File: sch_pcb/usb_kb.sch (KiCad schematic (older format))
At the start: 44 parts, among them J1 Conn_01x04_Female, P1 USB_C_Plug, SW1 SW_Push, SW2 SW_Push, U1 STM32F103C6Tx, U2 USBLC6-2SC6, U3 AMS1117-3.3, X1 8MHz

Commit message: Новые посадочные места
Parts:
- C1, C10, C11, C12, C13, C14, C15, C2, C3, C4, C5, C6, C7, C8, C9: footprint Capacitor_SMD:C_0805_2012Metric_Pad1.15x1.40mm_HandSolder -> Capacitor_SMD:C_0805_2012Metric_Pad1.18x1.45mm_HandSolder
- R1, R10, R11, R12, R13, R14, R15, R2, R3, R4, R5, R6, R7, R8, R9: footprint Resistor_SMD:R_0603_1608Metric_Pad1.05x0.95mm_HandSolder -> Resistor_SMD:R_0805_2012Metric_Pad1.20x1.40mm_HandSolder
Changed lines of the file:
@@
 F 0 "R1" V 3343 2050 50  0000 C CNN
 F 1 "20R" V 3434 2050 50  0000 C CNN
-F 2 "Resistor_SMD:R_0603_1608Metric_Pad1.05x0.95mm_HandSolder" V 3480 2050 50  0001 C CNN
+F 2 "Resistor_SMD:R_0805_2012Metric_Pad1.20x1.40mm_HandSolder" V 3480 2050 50  0001 C CNN
 F 3 "~" H 3550 2050 50  0001 C CNN
 	1    3550 2050
@@
 F 0 "R2" V 3343 3350 50  0000 C CNN
 F 1 "R" V 3434 3350 50  0000 C CNN
-F 2 "Resistor_SMD:R_0603_1608Metric_Pad1.05x0.95mm_HandSolder" V 3480 3350 50  0001 C CNN
+F 2 "Resistor_SMD:R_0805_2012Metric_Pad1.20x1.40mm_HandSolder" V 3480 3350 50  0001 C CNN
 F 3 "~" H 3550 3350 50  0001 C CNN
 	1    3550 3350
@@
 F 0 "C2" H 3565 4246 50  0000 L CNN
 F 1 "0.1uF" H 3565 4155 50  0000 L CNN
-F 2 "Capacitor_SMD:C_0805_2012Metric_Pad1.15x1.40mm_HandSolder" H 3488 4050 50  0001 C CNN
+F 2 "Capacitor_SMD:C_0805_2012Metric_Pad1.18x1.45mm_HandSolder" H 3488 4050 50  0001 C CNN
 F 3 "~" H 3450 4200 50  0001 C CNN
 	1    3450 4200
@@
 F 0 "C1" H 3215 4246 50  0000 L CNN
 F 1 "1uF" H 3215 4155 50  0000 L CNN
-F 2 "Capacitor_SMD:C_0805_2012Metric_Pad1.15x1.40mm_HandSolder" H 3138 4050 50  0001 C CNN
+F 2 "Capacitor_SMD:C_0805_2012Metric_Pad1.18x1.45mm_HandSolder" H 3138 4050 50  0001 C CNN
 F 3 "~" H 3100 4200 50  0001 C CNN
 	1    3100 4200
@@
 F 0 "C4" H 5015 4246 50  0000 L CNN
 F 1 "0.1uF" H 5015 4155 50  0000 L CNN
-F 2 "Capacitor_SMD:C_0805_2012Metric_Pad1.15x1.40mm_HandSolder" H 4938 4050 50  0001 C CNN
+F 2 "Capacitor_SMD:C_0805_2012Metric_Pad1.18x1.45mm_HandSolder" H 4938 4050 50  0001 C CNN
 F 3 "~" H 4900 4200 50  0001 C CNN
 	1    4900 4200
@@
 F 0 "C3" H 4665 4246 50  0000 L CNN
 F 1 "1uF" H 4665 4155 50  0000 L CNN
-F 2 "Capacitor_SMD:C_0805_2012Metric_Pad1.15x1.40mm_HandSolder" H 4588 4050 50  0001 C CNN
+F 2 "Capacitor_SMD:C_0805_2012Metric_Pad1.18x1.45mm_HandSolder" H 4588 4050 50  0001 C CNN
 F 3 "~" H 4550 4200 50  0001 C CNN
 	1    4550 4200
@@
 F 0 "C5" H 4315 1146 50  0000 L CNN
 F 1 "100nF" H 4315 1055 50  0000 L CNN
-F 2 "Capacitor_SMD:C_0805_2012Metric_Pad1.15x1.40mm_HandSolder" H 4238 950 50  0001 C CNN
+F 2 "Capacitor_SMD:C_0805_2012Metric_Pad1.18x1.45mm_HandSolder" H 4238 950 50  0001 C CNN
 F 3 "~" H 4200 1100 50  0001 C CNN
 	1    4200 1100
@@
 F 0 "C6" H 4765 1146 50  0000 L CNN
 F 1 "100nF" H 4765 1055 50  0000 L CNN
-F 2 "Capacitor_SMD:C_0805_2012Metric_Pad1.15x1.40mm_HandSolder" H 4688 950 50  0001 C CNN
+F 2 "Capacitor_SMD:C_0805_2012Metric_Pad1.18x1.45mm_HandSolder" H 4688 950 50  0001 C CNN
 F 3 "~" H 4650 1100 50  0001 C CNN
 	1    4650 1100
@@
 F 0 "C7" H 5165 1146 50  0000 L CNN
 F 1 "100nF" H 5165 1055 50  0000 L CNN
-F 2 "Capacitor_SMD:C_0805_2012Metric_Pad1.15x1.40mm_HandSolder" H 5088 950 50  0001 C CNN
+F 2 "Capacitor_SMD:C_0805_2012Metric_Pad1.18x1.45mm_HandSolder" H 5088 950 50  0001 C CNN
 F 3 "~" H 5050 1100 50  0001 C CNN
 	1    5050 1100
@@
 F 0 "C8" H 5615 1146 50  0000 L CNN
 F 1 "100nF" H 5615 1055 50  0000 L CNN
-F 2 "Capacitor_SMD:C_0805_2012Metric_Pad1.15x1.40mm_HandSolder" H 5538 950 50  0001 C CNN
+F 2 "Capacitor_SMD:C_0805_2012Metric_Pad1.18x1.45mm_HandSolder" H 5538 950 50  0001 C CNN
 F 3 "~" H 5500 1100 50  0001 C CNN
 	1    5500 1100
@@
 F 0 "C9" V 6198 2300 50  0000 C CNN
 F 1 "20pF" V 6289 2300 50  0000 C CNN
-F 2 "Capacitor_SMD:C_0805_2012Metric_Pad1.15x1.40mm_HandSolder" H 6488 2150 50  0001 C CNN
+F 2 "Capacitor_SMD:C_0805_2012Metric_Pad1.18x1.45mm_HandSolder" H 6488 2150 50  0001 C CNN
 F 3 "~" H 6450 2300 50  0001 C CNN
 	1    6450 2300
@@
 F 0 "R4" H 7320 2646 50  0000 L CNN
 F 1 "1M" H 7320 2555 50  0000 L CNN
-F 2 "Resistor_SMD:R_0603_1608Metric_Pad1.05x0.95mm_HandSolder" V 7180 2600 50  0001 C CNN
+F 2 "Resistor_SMD:R_0805_2012Metric_Pad1.20x1.40mm_HandSolder" V 7180 2600 50  0001 C CNN
 F 3 "~" H 7250 2600 50  0001 C CNN
 	1    7250 2600
@@
 F 0 "C10" V 6198 2900 50  0000 C CNN
 F 1 "20pF" V 6289 2900 50  0000 C CNN
-F 2 "Capacitor_SMD:C_0805_2012Metric_Pad1.15x1.40mm_HandSolder" H 6488 2750 50  0001 C CNN
+F 2 "Capacitor_SMD:C_0805_2012Metric_Pad1.18x1.45mm_HandSolder" H 6488 2750 50  0001 C CNN
 F 3 "~" H 6450 2900 50  0001 C CNN
 	1    6450 2900
@@
 F 0 "C11" H 7165 1596 50  0000 L CNN
 F 1 "100nF" H 7165 1505 50  0000 L CNN
-F 2 "Capacitor_SMD:C_0805_2012Metric_Pad1.15x1.40mm_HandSolder" H 7088 1400 50  0001 C CNN
+F 2 "Capacitor_SMD:C_0805_2012Metric_Pad1.18x1.45mm_HandSolder" H 7088 1400 50  0001 C CNN
 F 3 "~" H 7050 1550 50  0001 C CNN
 	1    7050 1550
@@
 F 0 "R3" H 7120 1146 50  0000 L CNN
 F 1 "10k" H 7120 1055 50  0000 L CNN
-F 2 "Resistor_SMD:R_0603_1608Metric_Pad1.05x0.95mm_HandSolder" V 6980 1100 50  0001 C CNN
+F 2 "Resistor_SMD:R_0805_2012Metric_Pad1.20x1.40mm_HandSolder" V 6980 1100 50  0001 C CNN
 F 3 "~" H 7050 1100 50  0001 C CNN
 	1    7050 1100
@@
 F 0 "R5" V 3593 3050 50  0000 C CNN
 F 1 "1.5k" V 3684 3050 50  0000 C CNN
-F 2 "Resistor_SMD:R_0603_1608Metric_Pad1.05x0.95mm_HandSolder" V 3730 3050 50  0001 C CNN
+F 2 "Resistor_SMD:R_0805_2012Metric_Pad1.20x1.40mm_HandSolder" V 3730 3050 50  0001 C CNN
 F 3 "~" H 3800 3050 50  0001 C CNN
 	1    3800 3050
@@
 F 0 "C13" H 5415 3646 50  0000 L CNN
 F 1 "47nF" H 5415 3555 50  0000 L CNN
-F 2 "Capacitor_SMD:C_0805_2012Metric_Pad1.15x1.40mm_HandSolder" H 5338 3450 50  0001 C CNN
+F 2 "Capacitor_SMD:C_0805_2012Metric_Pad1.18x1.45mm_HandSolder" H 5338 3450 50  0001 C CNN
 F 3 "~" H 5300 3600 50  0001 C CNN
 	1    5300 3600
@@
 F 0 "C12" H 5415 2346 50  0000 L CNN
 F 1 "47nF" H 5415 2255 50  0000 L CNN
-F 2 "Capacitor_SMD:C_0805_2012Metric_Pad1.15x1.40mm_HandSolder" H 5338 2150 50  0001 C CNN
+F 2 "Capacitor_SMD:C_0805_2012Metric_Pad1.18x1.45mm_HandSolder" H 5338 2150 50  0001 C CNN
 F 3 "~" H 5300 2300 50  0001 C CNN
 	1    5300 2300
@@
 F 0 "R6" V 5743 4100 50  0000 C CNN
 F 1 "10k" V 5834 4100 50  0000 C CNN
-F 2 "Resistor_SMD:R_0603_1608Metric_Pad1.05x0.95mm_HandSolder" V 5880 4100 50  0001 C CNN
+F 2 "Resistor_SMD:R_0805_2012Metric_Pad1.20x1.40mm_HandSolder" V 5880 4100 50  0001 C CNN
 F 3 "~" H 5950 4100 50  0001 C CNN
 	1    5950 4100
@@
 F 0 "R7" V 8007 3250 50  0000 C CNN
 F 1 "510" V 7916 3250 50  0000 C CNN
-F 2 "Resistor_SMD:R_0603_1608Metric_Pad1.05x0.95mm_HandSolder" V 7730 3250 50  0001 C CNN
+F 2 "Resistor_SMD:R_0805_2012Metric_Pad1.20x1.40mm_HandSolder" V 7730 3250 50  0001 C CNN
 F 3 "~" H 7800 3250 50  0001 C CNN
 	1    7800 3250
@@
 F 0 "R9" V 8007 4100 50  0000 C CNN
 F 1 "510" V 7916 4100 50  0000 C CNN
-F 2 "Resistor_SMD:R_0603_1608Metric_Pad1.05x0.95mm_HandSolder" V 7730 4100 50  0001 C CNN
+F 2 "Resistor_SMD:R_0805_2012Metric_Pad1.20x1.40mm_HandSolder" V 7730 4100 50  0001 C CNN
 F 3 "~" H 7800 4100 50  0001 C CNN
 	1    7800 4100
@@
 F 0 "R10" V 10557 1200 50  0000 C CNN
 F 1 "100" V 10466 1200 50  0000 C CNN
-F 2 "Resistor_SMD:R_0603_1608Metric_Pad1.05x0.95mm_HandSolder" V 10280 1200 50  0001 C CNN
+F 2 "Resistor_SMD:R_0805_2012Metric_Pad1.20x1.40mm_HandSolder" V 10280 1200 50  0001 C CNN
 F 3 "~" H 10350 1200 50  0001 C CNN
 	1    10350 1200
@@
 F 0 "R11" V 10907 2200 50  0000 C CNN
 F 1 "10k" V 10816 2200 50  0000 C CNN
-F 2 "Resistor_SMD:R_0603_1608Metric_Pad1.05x0.95mm_HandSolder" V 10630 2200 50  0001 C CNN
+F 2 "Resistor_SMD:R_0805_2012Metric_Pad1.20x1.40mm_HandSolder" V 10630 2200 50  0001 C CNN
 F 3 "~" H 10700 2200 50  0001 C CNN
 	1    10700 2200
@@
 F 0 "C14" V 10098 1650 50  0000 C CNN
 F 1 "0.1uF" V 10189 1650 50  0000 C CNN
-F 2 "Capacitor_SMD:C_0805_2012Metric_Pad1.15x1.40mm_HandSolder" H 10388 1500 50  0001 C CNN
+F 2 "Capacitor_SMD:C_0805_2012Metric_Pad1.18x1.45mm_HandSolder" H 10388 1500 50  0001 C CNN
 F 3 "~" H 10350 1650 50  0001 C CNN
 	1    10350 1650
@@
 F 0 "R8" V 8007 3600 50  0000 C CNN
 F 1 "510" V 7916 3600 50  0000 C CNN
-F 2 "Resistor_SMD:R_0603_1608Metric_Pad1.05x0.95mm_HandSolder" V 7730 3600 50  0001 C CNN
+F 2 "Resistor_SMD:R_0805_2012Metric_Pad1.20x1.40mm_HandSolder" V 7730 3600 50  0001 C CNN
 F 3 "~" H 7800 3600 50  0001 C CNN
 	1    7800 3600
@@
 F 0 "R13" V 10907 4250 50  0000 C CNN
 F 1 "10k" V 10816 4250 50  0000 C CNN
-F 2 "Resistor_SMD:R_0603_1608Metric_Pad1.05x0.95mm_HandSolder" V 10630 4250 50  0001 C CNN
+F 2 "Resistor_SMD:R_0805_2012Metric_Pad1.20x1.40mm_HandSolder" V 10630 4250 50  0001 C CNN
 F 3 "~" H 10700 4250 50  0001 C CNN
 	1    10700 4250
@@
 F 0 "R12" V 10407 3350 50  0000 C CNN
 F 1 "100" V 10316 3350 50  0000 C CNN
-F 2 "Resistor_SMD:R_0603_1608Metric_Pad1.05x0.95mm_HandSolder" V 10130 3350 50  0001 C CNN
+F 2 "Resistor_SMD:R_0805_2012Metric_Pad1.20x1.40mm_HandSolder" V 10130 3350 50  0001 C CNN
 F 3 "~" H 10200 3350 50  0001 C CNN
 	1    10200 3350
@@
 F 0 "C15" V 9948 3750 50  0000 C CNN
 F 1 "0.1uF" V 10039 3750 50  0000 C CNN
-F 2 "Capacitor_SMD:C_0805_2012Metric_Pad1.15x1.40mm_HandSolder" H 10238 3600 50  0001 C CNN
+F 2 "Capacitor_SMD:C_0805_2012Metric_Pad1.18x1.45mm_HandSolder" H 10238 3600 50  0001 C CNN
 F 3 "~" H 10200 3750 50  0001 C CNN
 	1    10200 3750
@@
 F 0 "R15" H 7870 5996 50  0000 L CNN
 F 1 "10k" H 7870 5905 50  0000 L CNN
-F 2 "Resistor_SMD:R_0603_1608Metric_Pad1.05x0.95mm_HandSolder" V 7730 5950 50  0001 C CNN
+F 2 "Resistor_SMD:R_0805_2012Metric_Pad1.20x1.40mm_HandSolder" V 7730 5950 50  0001 C CNN
 F 3 "~" H 7800 5950 50  0001 C CNN
 	1    7800 5950
@@
 F 0 "R14" H 7470 6096 50  0000 L CNN
 F 1 "10k" H 7470 6005 50  0000 L CNN
-F 2 "Resistor_SMD:R_0603_1608Metric_Pad1.05x0.95mm_HandSolder" V 7330 6050 50  0001 C CNN
+F 2 "Resistor_SMD:R_0805_2012Metric_Pad1.20x1.40mm_HandSolder" V 7330 6050 50  0001 C CNN
 F 3 "~" H 7400 6050 50  0001 C CNN
 	1    7400 6050

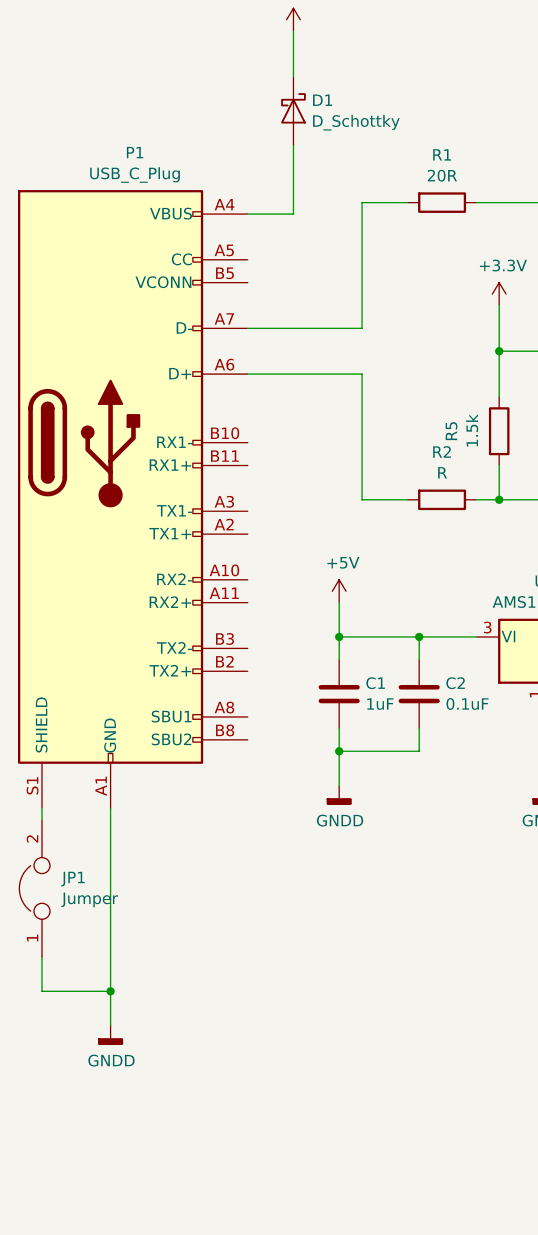
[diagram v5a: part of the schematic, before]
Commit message: Исправил посадочное место USB
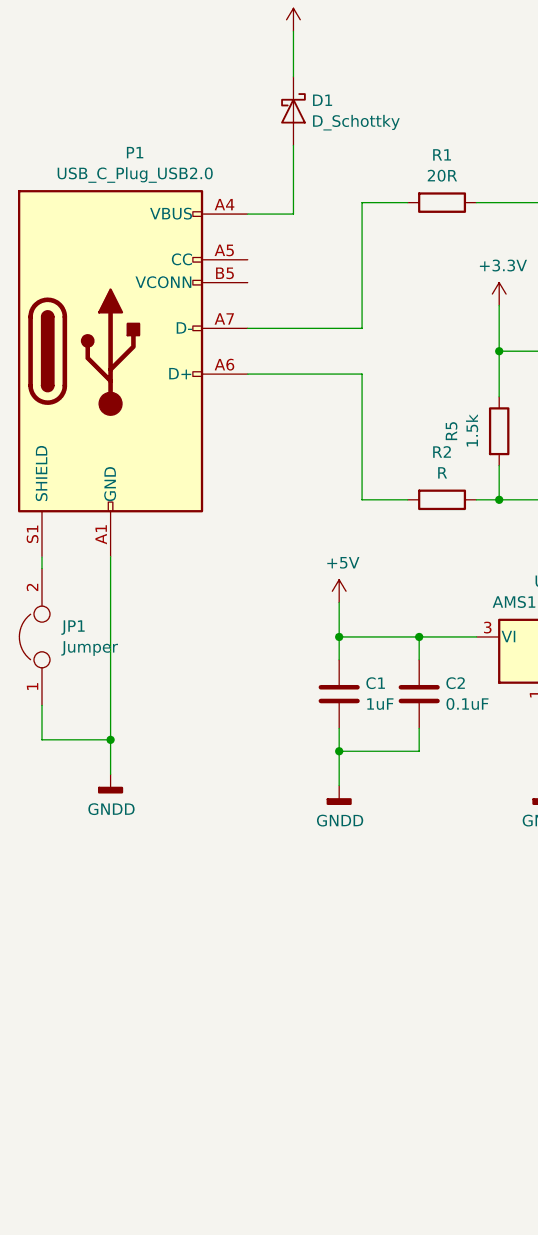
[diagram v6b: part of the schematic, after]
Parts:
- removed P1: USB_C_Plug, Connector_USB:USB_C_Receptacle_HRO_TYPE-C-31-M-12, symbol usb_kb-rescue:USB_C_Plug-Connector
- added P1: USB_C_Plug_USB2.0, Connector_USB:USB_C_Receptacle_HRO_TYPE-C-31-M-12, symbol Connector:USB_C_Plug_USB2.0
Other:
- moved on the sheet: JP1
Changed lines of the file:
@@
 $EndComp
 Wire Wire Line
-	2100 5500 2100 5650
-Connection ~ 2100 5500
-Wire Wire Line
-	1800 5500 2100 5500
-Wire Wire Line
-	1800 5500 1800 5350
-Wire Wire Line
-	2100 4700 2100 5500
-Wire Wire Line
-	1800 4700 1800 4750
+	2100 4400 2100 4550
+Connection ~ 2100 4400
+Wire Wire Line
+	1800 4400 2100 4400
+Wire Wire Line
+	1800 4400 1800 4250
+Wire Wire Line
+	2100 3600 2100 4400
+Wire Wire Line
+	1800 3600 1800 3650
 $Comp
 L Device:Jumper JP1
 U 1 1 615515A1
-P 1800 5050
-F 0 "JP1" V 1846 4962 50  0000 R CNN
-F 1 "Jumper" V 1755 4962 50  0000 R CNN
-F 2 "Jumper:SolderJumper-2_P1.3mm_Open_TrianglePad1.0x1.5mm" H 1800 5050 50  0001 C CNN
-F 3 "~" H 1800 5050 50  0001 C CNN
-	1    1800 5050
+P 1800 3950
+F 0 "JP1" V 1846 3862 50  0000 R CNN
+F 1 "Jumper" V 1755 3862 50  0000 R CNN
+F 2 "Jumper:SolderJumper-2_P1.3mm_Open_TrianglePad1.0x1.5mm" H 1800 3950 50  0001 C CNN
+F 3 "~" H 1800 3950 50  0001 C CNN
+	1    1800 3950
 	0    -1   -1   0
 $EndComp
@@
 L power:GNDD #PWR0103
 U 1 1 6154E00D
-P 2100 5650
-F 0 "#PWR0103" H 2100 5400 50  0001 C CNN
-F 1 "GNDD" H 2104 5495 50  0000 C CNN
-F 2 "" H 2100 5650 50  0001 C CNN
-F 3 "" H 2100 5650 50  0001 C CNN
-	1    2100 5650
-	1    0    0    -1
-$EndComp
-$Comp
-L usb_kb-rescue:USB_C_Plug-Connector P1
-U 1 1 6152BA8E
-P 2100 3100
-F 0 "P1" H 2207 4367 50  0000 C CNN
-F 1 "USB_C_Plug" H 2207 4276 50  0000 C CNN
-F 2 "Connector_USB:USB_C_Receptacle_HRO_TYPE-C-31-M-12" H 2250 3100 50  0001 C CNN
-F 3 "https://www.usb.org/sites/default/files/documents/usb_type-c.zip" H 2250 3100 50  0001 C CNN
-	1    2100 3100
+P 2100 4550
+F 0 "#PWR0103" H 2100 4300 50  0001 C CNN
+F 1 "GNDD" H 2104 4395 50  0000 C CNN
+F 2 "" H 2100 4550 50  0001 C CNN
+F 3 "" H 2100 4550 50  0001 C CNN
+	1    2100 4550
 	1    0    0    -1
 $EndComp
@@
 Wire Wire Line
 	7400 6200 7400 6300
+$Comp
+L Connector:USB_C_Plug_USB2.0 P1
+U 1 1 6159C626
+P 2100 2700
+F 0 "P1" H 2207 3567 50  0000 C CNN
+F 1 "USB_C_Plug_USB2.0" H 2207 3476 50  0000 C CNN
+F 2 "Connector_USB:USB_C_Receptacle_HRO_TYPE-C-31-M-12" H 2250 2700 50  0001 C CNN
+F 3 "https://www.usb.org/sites/default/files/documents/usb_type-c.zip" H 2250 2700 50  0001 C CNN
+	1    2100 2700
+	1    0    0    -1
+$EndComp
 $EndSCHEMATC

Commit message: Разработал схему
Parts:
- removed C6, C7, C8: 100nF, Capacitor_SMD:C_0805_2012Metric_Pad1.18x1.45mm_HandSolder, symbol Device:C
- removed D2, D4: LED_ALT, Diode_SMD:D_0805_2012Metric_Pad1.15x1.40mm_HandSolder, symbol Device:LED_ALT
- removed R7, R8: 510, Resistor_SMD:R_0805_2012Metric_Pad1.20x1.40mm_HandSolder, symbol Device:R
- C1, C10, C11, C12, C13, C14, C15, C2, C3, C4, C5, C9: footprint Capacitor_SMD:C_0805_2012Metric_Pad1.18x1.45mm_HandSolder -> Capacitor_SMD:C_0603_1608Metric_Pad1.05x0.95mm_HandSolder
- D1: footprint Diode_SMD:D_SMA -> Diode_SMD:D_MiniMELF_Handsoldering
- R1, R10, R11, R12, R13, R14, R15, R2, R3, R4, R5, R6, R9: footprint Resistor_SMD:R_0805_2012Metric_Pad1.20x1.40mm_HandSolder -> Resistor_SMD:R_0603_1608Metric_Pad1.05x0.95mm_HandSolder
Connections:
- wire segments 167 -> 153

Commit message: Переделал схему, добавил дифф пару
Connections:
- net labels added: D_N, D_P, USB_N, USB_P
- net labels removed: USB_D+, USB_D-
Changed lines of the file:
@@
 Comment4 ""
 $EndDescr
-Wire Wire Line
-	4450 3350 4650 3350
-Wire Wire Line
-	4450 2050 4650 2050
 $Comp
 L power:+5V #PWR0101
@@
 	1    0    0    -1
 $EndComp
-Wire Wire Line
-	5100 2700 5100 2900
 $Comp
 L Device:R R1
@@
 	0    1    1    0
 $EndComp
-Connection ~ 4650 3350
-Connection ~ 4650 2050
 Text Label 5550 2050 0    50   ~ 0
-USB_D-
+USB_N
 Text Label 5550 3350 0    50   ~ 0
-USB_D+
+USB_P
 $Comp
 L Device:C C2
@@
 $EndComp
 Text Label 9900 4350 0    50   ~ 0
-USB_D-
+USB_N
 Text Label 9900 4450 0    50   ~ 0
-USB_D+
+USB_P
 Wire Wire Line
 	9600 4350 9900 4350
@@
 Wire Wire Line
 	3700 3350 3800 3350
-Connection ~ 4450 3350
 Wire Wire Line
 	3800 3200 3800 3350
 Connection ~ 3800 3350
-Wire Wire Line
-	3800 3350 4450 3350
-Wire Wire Line
-	3800 2700 3800 2900
-Wire Wire Line
-	3800 2700 3800 2500
-Connection ~ 3800 2700
-Wire Wire Line
-	3700 2050 4450 2050
-Connection ~ 4450 2050
-Wire Wire Line
-	4650 3350 5300 3350
-Wire Wire Line
-	4650 2050 5300 2050
 $Comp
 L Device:C C13
@@
 	0    -1   -1   0
 $EndComp
-Wire Wire Line
-	4450 2050 4450 2300
-Wire Wire Line
-	4650 2050 4650 2300
-Wire Wire Line
-	4950 2700 5100 2700
-Wire Wire Line
-	4650 3100 4650 3350
-Wire Wire Line
-	4450 3100 4450 3350
-Wire Wire Line
-	3800 2700 4150 2700
 $Comp
 L Switch:SW_Push SW2
@@
 Wire Wire Line
 	7400 6200 7400 6300
+Text Label 2850 2600 0    50   ~ 0
+D_N
+Text Label 2850 2800 0    50   ~ 0
+D_P
 $Comp
 L Connector:USB_C_Plug_USB2.0 P1
@@
 	1    0    0    -1
 $EndComp
+Wire Wire Line
+	3800 2500 3800 2700
+Wire Wire Line
+	3800 3350 4450 3350
+Wire Wire Line
+	3700 2050 4450 2050
+Wire Wire Line
+	4450 2200 4450 2050
+Connection ~ 4450 2050
+Wire Wire Line
+	4450 2050 4650 2050
+Wire Wire Line
+	4650 2200 4650 2050
+Connection ~ 4650 2050
+Wire Wire Line
+	4650 2050 5300 2050
+Wire Wire Line
+	4050 2700 3800 2700
+Connection ~ 3800 2700
+Wire Wire Line
+	3800 2700 3800 2900
+Wire Wire Line
+	5050 2700 5100 2700
+Wire Wire Line
+	5100 2700 5100 2900
+Wire Wire Line
+	4450 3200 4450 3350
+Connection ~ 4450 3350
+Wire Wire Line
+	4450 3350 4650 3350
+Wire Wire Line
+	4650 3200 4650 3350
+Connection ~ 4650 3350
+Wire Wire Line
+	4650 3350 5300 3350
 $EndSCHEMATC
